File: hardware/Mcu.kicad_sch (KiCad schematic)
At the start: 22 parts, among them U1 STM32G484RETx, Y1 X322516MLB4SI, Y2 Q13FC1350000400

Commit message: fixed some footprints; shorted pcb board to 60x100; re-designed the HV & current measuring as well as LTC communication, all are in one TS section;
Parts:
- C23: value 10uF -> 22uF; footprint Capacitor_SMD:C_0603_1608Metric -> Capacitor_SMD:C_0805_2012Metric
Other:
- note removed: "Clocks"
- note removed: "IO power filtraton"
- note removed: "MCU"
- note removed: "Miscellaneous"
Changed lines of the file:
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@@
 		)
 	)
-	(text "IO power filtraton"
-		(exclude_from_sim no)
-		(at 50.8 146.05 0)
-		(effects
-			(font
-				(size 5 5)
-				(thickness 1)
-				(bold yes)
-			)
-			(justify left bottom)
-		)
-	)
-	(text "Clocks"
-		(exclude_from_sim no)
-		(at 62.23 35.56 0)
-		(effects
-			(font
-				(size 5 5)
-				(thickness 1)
-				(bold yes)
-			)
-			(justify left bottom)
-		)
-	)
-	(text "MCU"
-		(exclude_from_sim no)
-		(at 212.09 43.18 0)
-		(effects
-			(font
-				(size 5 5)
-				(thickness 1)
-				(bold yes)
-			)
-			(justify left bottom)
-		)
-	)
-	(text "Miscellaneous"
-		(exclude_from_sim no)
-		(at 53.34 93.98 0)
-		(effects
-			(font
-				(size 5 5)
-				(thickness 1)
-				(bold yes)
-			)
-			(justify left bottom)
-		)
-	)
 	(label "RTC_CLK_OUT"
 		(at 90.17 55.88 0)
@@
 			)
 		)
-		(property "Value" "10uF"
+		(property "Value" "22uF"
 			(at 90.17 180.1114 0)
 			(effects
@@
 			)
 		)
-		(property "Footprint" "Capacitor_SMD:C_0603_1608Metric"
+		(property "Footprint" "Capacitor_SMD:C_0805_2012Metric"
 			(at 92.71 179.07 0)
 			(effects

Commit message: sync
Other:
- note added: "CLOCKS"
- note added: "LEDS"
- note added: "POWER"
- note added: "PULL-UPS"
- note added: "uC"
- moved on the sheet: C1, C2, C23, C24, C25, C28, C29, C3, C4, D1, D2, D3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

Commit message: sync
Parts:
- removed D1, D2, D3: SML-D12U1WT86, LED_SMD:LED_0603_1608Metric, symbol Device:LED_Small_ALT
- removed R1, R2, R3: 1k, Resistor_SMD:R_0603_1608Metric, symbol Device:R_Small
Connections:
- net LTC_1_~{CS} renamed ~{LTC_CS}
- net LTC_2_~{CS} renamed ~{ADC_DRY}
- net MES_MISO renamed ADC_MISO
- net MES_MOSI renamed ADC_MOSI
- net MES_SCK renamed ADC_SCK
- net ~{MES_EXT_I_CS}: no longer names the net of U1.44 (PA10)
- net ~{MES_EXT_V_CS} renamed ~{EXT_CS}
- net ~{MES_I_SENS_CS}: no longer names the net of U1.42 (PA8)
- net ~{MES_V_ACU_CS} renamed ~{ADC_CS}
- net ~{MES_V_CAR_CS}: no longer names the net of U1.55 (PD2)
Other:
- note added: "MCU"
- note removed: "LEDS"
- note removed: "uC"
- moved on the sheet: C1, C2, C3, C4, R4, R5, R6, Y1, Y2

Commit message: schematic done
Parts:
- removed R4, R5, R6: 1k, Resistor_SMD:R_0603_1608Metric, symbol Device:R_Small
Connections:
- net SIGNAL_AMS_FAULT: now also U1.44 (PA10); no longer U1.51 (PA15)
- net ~{ADC_CS}: now also U1.51 (PA15); no longer U1.60 (PB7)
- net ~{EXT_CS}: now also U1.18 (PA4); no longer U1.43 (PA9)
- net EXT_SCK: now reaches U1.19 (PA5)
- net EXT_MISO: now reaches U1.20 (PA6)
- net EXT_MOSI: now reaches U1.21 (PA7)
- net +3V3 renamed +3.3V
- net BOOT renamed BOOT0
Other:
- note removed: "PULL-UPS"
- moved on the sheet: C1, C2, C3, C4, Y1, Y2

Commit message: new firmware for bga version of stm, change stm from smt to bga, smaller HV dividers, added 3rd can transciver, and other
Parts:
- removed C3, C4: 25pF, Capacitor_SMD:C_0603_1608Metric, symbol Device:C_Small
- removed L3: 4.7uH, Inductor_SMD:L_1206_3216Metric, symbol Device:L_Small
- removed U1: STM32G484RETx, Package_QFP:LQFP-64_10x10mm_P0.5mm, symbol MCU_ST_STM32G4:STM32G484RETx
- removed Y2: Q13FC1350000400, Crystal:Crystal_SMD_3215-2Pin_3.2x1.5mm, symbol Device:Crystal_Small
- added R4: 0, Resistor_SMD:R_0603_1608Metric, symbol Device:R_Small
- added U10: STM32G484VEHx, Package_BGA:TFBGA-100_8x8mm_Layout10x10_P0.8mm, symbol MCU_ST_STM32G4:STM32G484VEHx
- C23: value 22uF -> 100nF; footprint Capacitor_SMD:C_0805_2012Metric -> Capacitor_SMD:C_0603_1608Metric
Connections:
- net +3.3V: now also R4.2; no longer C24.1, C25.1, C28.1, C29.1
- net GND: now also U10.D2 (VSS), U10.D6 (VSS), U10.E5 (VSS), U10.E6 (VSS), U10.E7 (VSS), U10.F6 (VSS), U10.K4 (VSSA)
- net VIO: now reaches C23.1
- net VIO: now also C24.1, C25.1, C28.1, C29.1, R4.1, U10.D5 (VDD), U10.D7 (VDD), U10.F5 (VDD), U10.F7 (VDD), U10.J5 (VDDA), U10.K5 (VREF+)
- no-connect marks 6 -> 2
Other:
- moved on the sheet: C1, C2, Y1

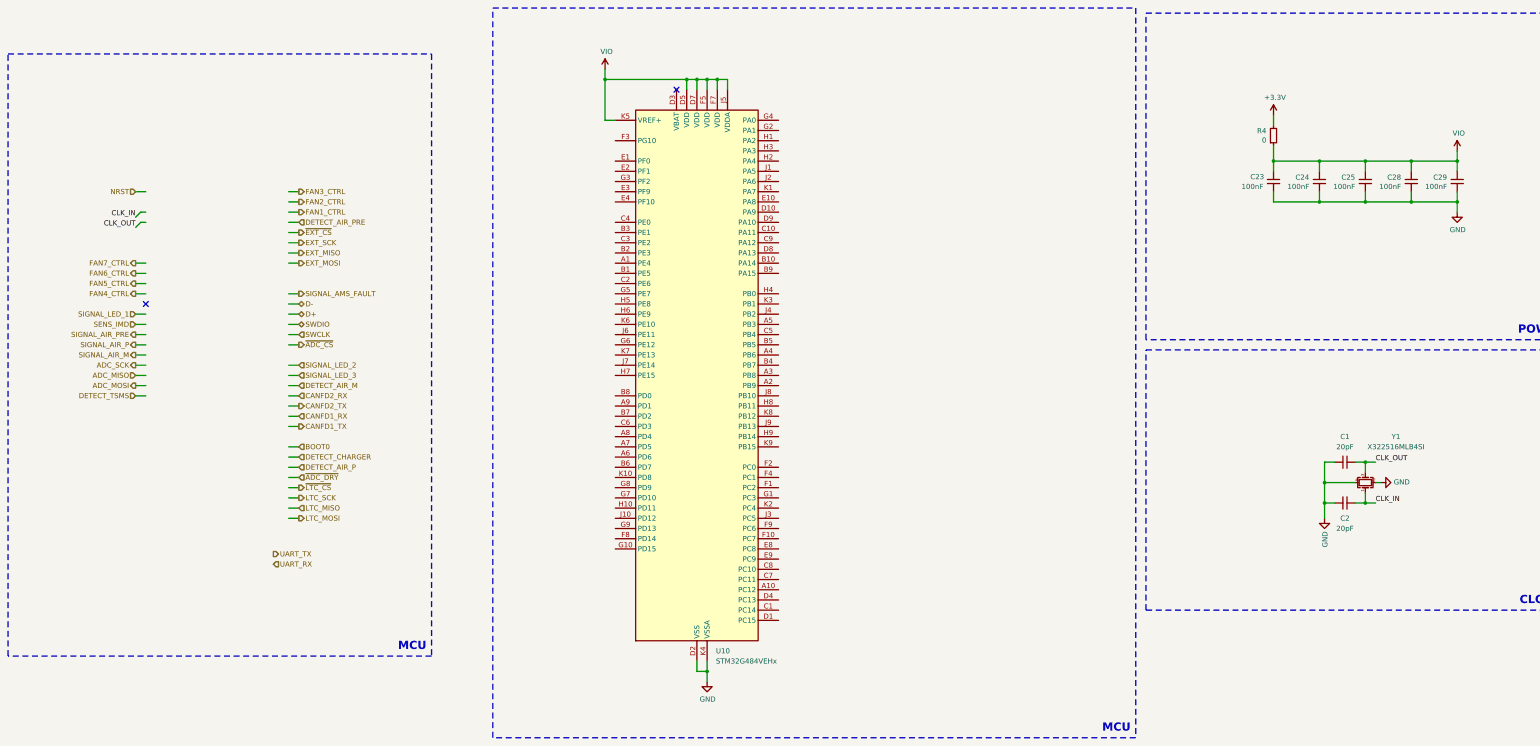
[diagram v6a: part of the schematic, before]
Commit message: mcu pinout done
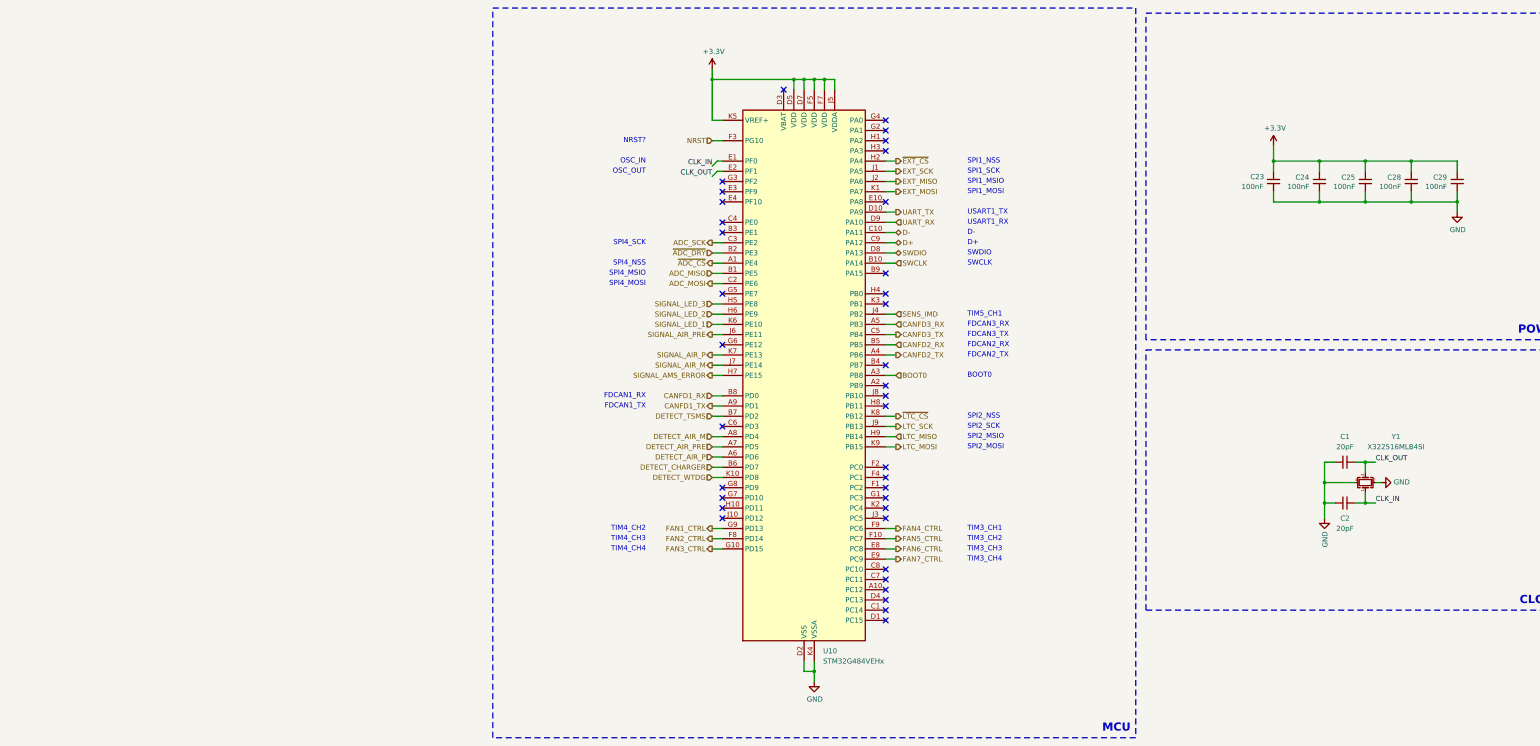
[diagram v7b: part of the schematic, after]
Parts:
- removed R4: 0, Resistor_SMD:R_0603_1608Metric, symbol Device:R_Small
- C23, C24, C25, C28, C29: footprint Capacitor_SMD:C_0603_1608Metric -> Capacitor_SMD:C_0402_1005Metric
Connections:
- net VIO is gone; now on net +3.3V: C23.1, C24.1, C25.1, C28.1, C29.1, U10.D5 (VDD), U10.D7 (VDD), U10.F5 (VDD), U10.F7 (VDD), U10.J5 (VDDA), U10.K5 (VREF+)
- net ADC_MISO: now also U10.B1 (PE5)
- net ADC_MOSI: now also U10.C2 (PE6)
- net ADC_SCK: now also U10.C3 (PE2)
- net BOOT0: now also U10.A3 (PB8)
- net CANFD1_RX: now also U10.B8 (PD0)
- net CANFD1_TX: now also U10.A9 (PD1)
- net CANFD2_RX: now also U10.B5 (PB5)
- net CANFD2_TX: now also U10.A4 (PB6)
- net CLK_IN: now also U10.E1 (PF0)
- net CLK_OUT: now also U10.E2 (PF1)
- net D+: now also U10.C9 (PA12)
- net D-: now also U10.C10 (PA11)
- net DETECT_AIR_M: now also U10.A8 (PD4)
- net DETECT_AIR_P: now also U10.A6 (PD6)
- net DETECT_AIR_PRE: now also U10.A7 (PD5)
- net DETECT_CHARGER: now also U10.B6 (PD7)
- net DETECT_TSMS: now also U10.B7 (PD2)
- net EXT_MISO: now also U10.J2 (PA6)
- net EXT_MOSI: now also U10.K1 (PA7)
- net EXT_SCK: now also U10.J1 (PA5)
- net FAN1_CTRL: now also U10.G9 (PD13)
- net FAN2_CTRL: now also U10.F8 (PD14)
- net FAN3_CTRL: now also U10.G10 (PD15)
- net FAN4_CTRL: now also U10.F9 (PC6)
- net FAN5_CTRL: now also U10.F10 (PC7)
- net FAN6_CTRL: now also U10.E8 (PC8)
- net FAN7_CTRL: now also U10.E9 (PC9)
- net LTC_MISO: now also U10.H9 (PB14)
- net LTC_MOSI: now also U10.K9 (PB15)
- net LTC_SCK: now also U10.J9 (PB13)
- net NRST: now also U10.F3 (PG10)
- net SENS_IMD: now also U10.J4 (PB2)
- net SIGNAL_AIR_M: now also U10.J7 (PE14)
- net SIGNAL_AIR_P: now also U10.K7 (PE13)
- net SIGNAL_AIR_PRE: now also U10.J6 (PE11)
- net SIGNAL_LED_1: now also U10.K6 (PE10)
- net SIGNAL_LED_2: now also U10.H6 (PE9)
- net SIGNAL_LED_3: now also U10.H5 (PE8)
- net SWCLK: now also U10.B10 (PA14)
- net SWDIO: now also U10.D8 (PA13)
- net UART_RX: now also U10.D9 (PA10)
- net UART_TX: now also U10.D10 (PA9)
- net ~{ADC_CS}: now also U10.A1 (PE4)
- net ~{ADC_DRY}: now also U10.B2 (PE3)
- net ~{EXT_CS}: now also U10.H2 (PA4)
- net ~{LTC_CS}: now also U10.K8 (PB12)
- net CANFD3_RX: now reaches U10.A5 (PB3)
- net CANFD3_TX: now reaches U10.C5 (PB4)
- net SIGNAL_AMS_ERROR: now reaches U10.H7 (PE15)
- net DETECT_WTDG: now reaches U10.K10 (PD8)
- no-connect marks 2 -> 37
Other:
- note added: "BOOT0"
- note added: "D+"
- note added: "D-"
- note added: "FDCAN1_RX"
- note added: "FDCAN1_TX"
- note added: "FDCAN2_RX"
- note added: "FDCAN2_TX"
- note added: "FDCAN3_RX"
- note added: "FDCAN3_TX"
- note added: "NRST?"
- note added: "OSC_IN"
- note added: "OSC_OUT"
- note added: "SPI1_MOSI"
- note added: "SPI1_MSIO"
- note added: "SPI1_NSS"
- note added: "SPI1_SCK"
- note added: "SPI2_MOSI"
- note added: "SPI2_MSIO"
- note added: "SPI2_NSS"
- note added: "SPI2_SCK"
- note added: "SPI4_MOSI"
- note added: "SPI4_MSIO"
- note added: "SPI4_NSS"
- note added: "SPI4_SCK"
- note added: "SWCLK"
- note added: "SWDIO"
- note added: "TIM3_CH1"
- note added: "TIM3_CH2"
- note added: "TIM3_CH3"
- note added: "TIM3_CH4"
- note added: "TIM4_CH2"
- note added: "TIM4_CH3"
- note added: "TIM4_CH4"
- note added: "TIM5_CH1"
- note added: "USART1_RX"
- note added: "USART1_TX"
- moved on the sheet: U10

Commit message: mama comit
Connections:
- net BOOT0: no longer names the net of U10.A3 (PB8)
- no-connect marks 37 -> 38
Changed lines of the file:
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@@
+	)
+	(no_connect
+		(at 111.76 105.41)
 	)
 	(no_connect
@@
 		(pts
 			(xy 242.57 59.69) (xy 242.57 62.23)
-		)
-		(stroke
-			(width 0)
-			(type default)
-		)
-	)
-	(wire
-		(pts
-			(xy 114.3 105.41) (xy 111.76 105.41)
 		)
 		(stroke
@@
 		)
 	)
-	(hierarchical_label "BOOT0"
-		(shape input)
-		(at 114.3 105.41 0)
-		(fields_autoplaced yes)
-		(effects
-			(font
-				(size 1.27 1.27)
-			)
-			(justify left)
-		)
-	)
